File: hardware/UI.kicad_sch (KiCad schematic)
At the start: 1 part

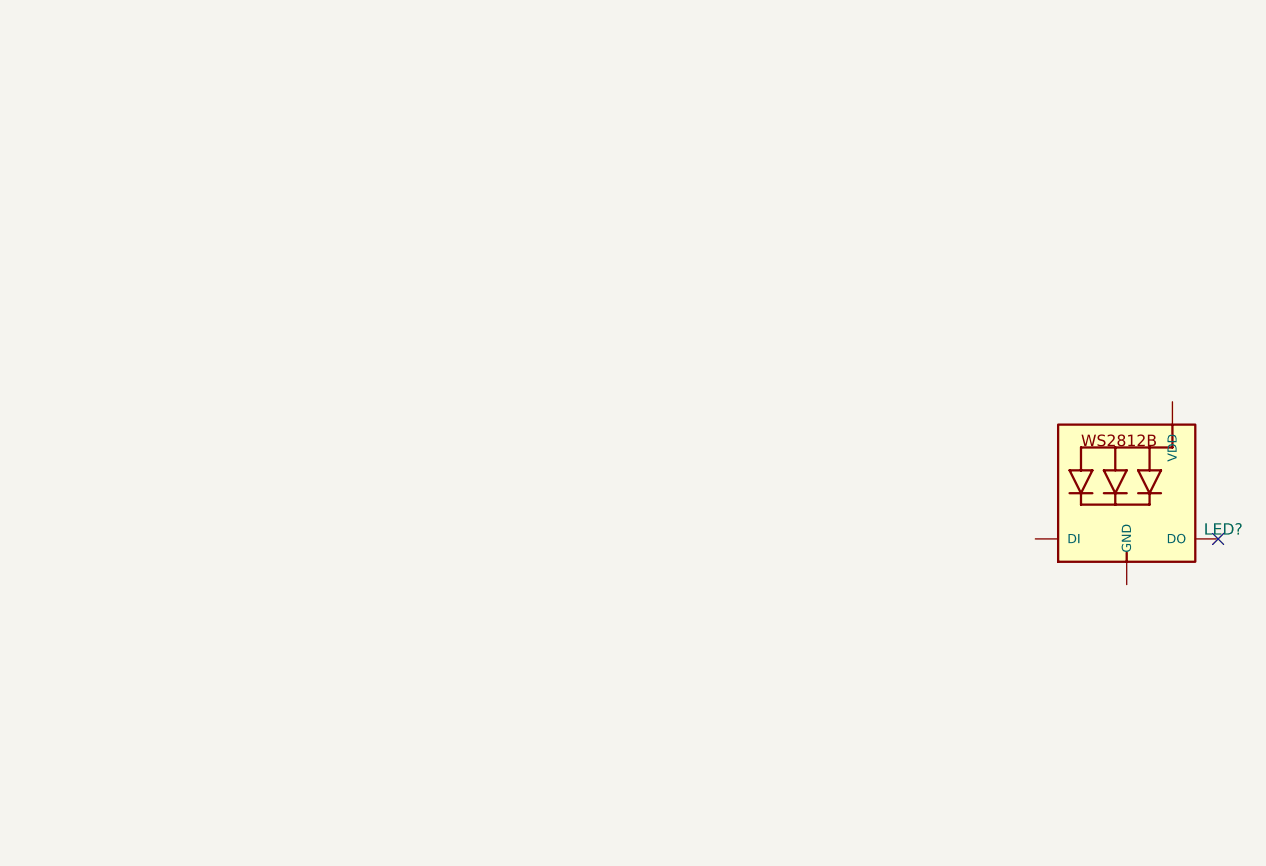
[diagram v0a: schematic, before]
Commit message: schematics finished, footprints assigned. Still need to fix foorptints for MOSFETS
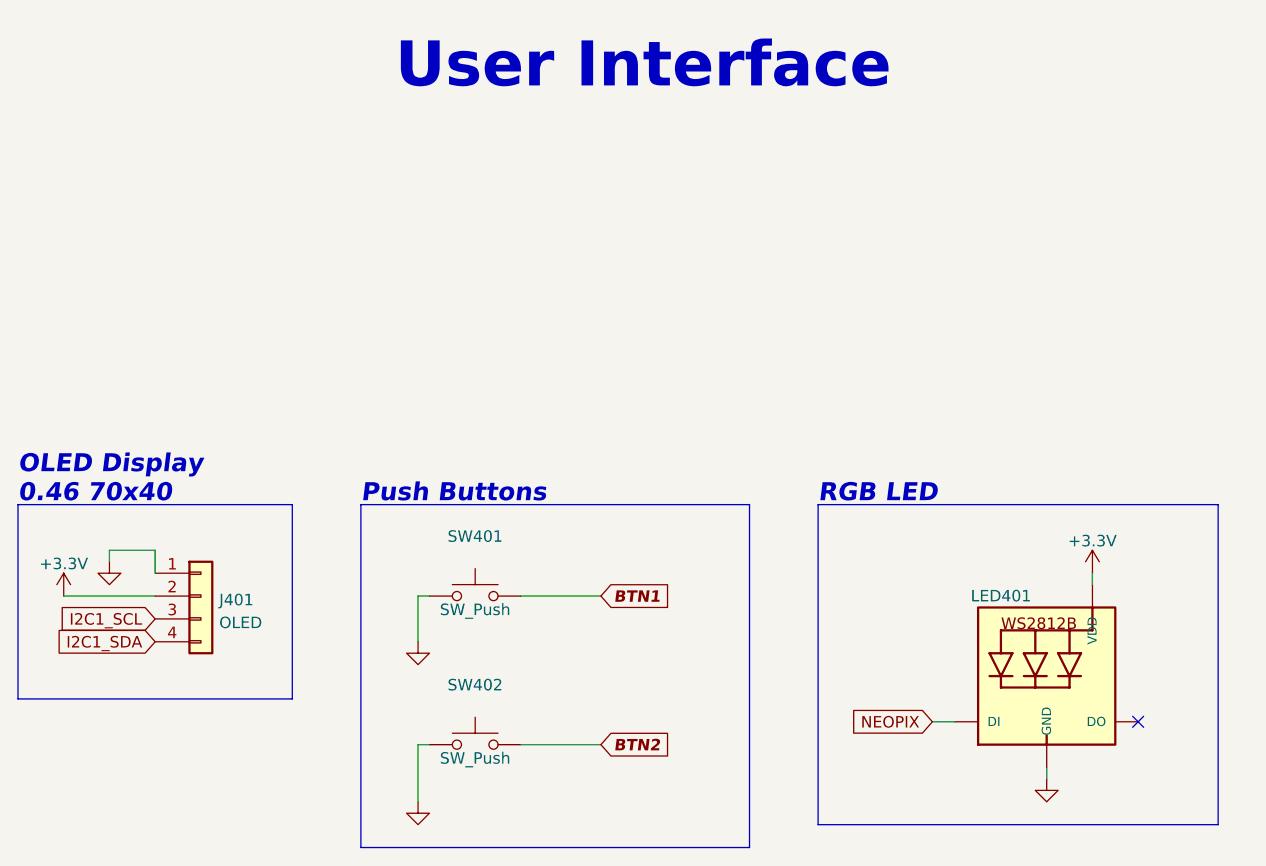
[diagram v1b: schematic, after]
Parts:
- added J401: OLED, Connector_PinHeader_2.54mm:PinHeader_1x04_P2.54mm_Vertical_SMD_Pin1Left, symbol Connector_Generic:Conn_01x04
- added SW401, SW402: SW_Push, STR-Switch:SW_SMD_SPST_8x3.6, symbol STR-Switches:SW_Push
- LED401: renamed from LED?; footprint (none) -> STR-LED:WS2812B; LCSC (none) -> C2761795; MANUFACTURER (none) -> WorldSemi; MFPN (none) -> WS2812B-B/W; MPN (none) -> WS2812B-B/W; Manufacturer (none) -> WorldSemi
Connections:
- new net +3V3: J401.2 (Pin_2), LED401.1 (VDD)
- new net BTN1: SW401.2
- new net BTN2: SW402.2
- new net GND: J401.1 (Pin_1), LED401.3 (GND), SW401.1, SW402.1
- new net I2C1_SCL: J401.3 (Pin_3)
- new net I2C1_SDA: J401.4 (Pin_4)
- new net NEOPIX: LED401.4 (DI)
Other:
- note added: "OLED Display 0.46 70x40"
- note added: "Push Buttons"
- note added: "RGB LED"
- note added: "User Interface"
- title: (none) -> SLA Chamber Hearter for Resin Printers
- moved on the sheet: LED401

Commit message: routing and foot print changes
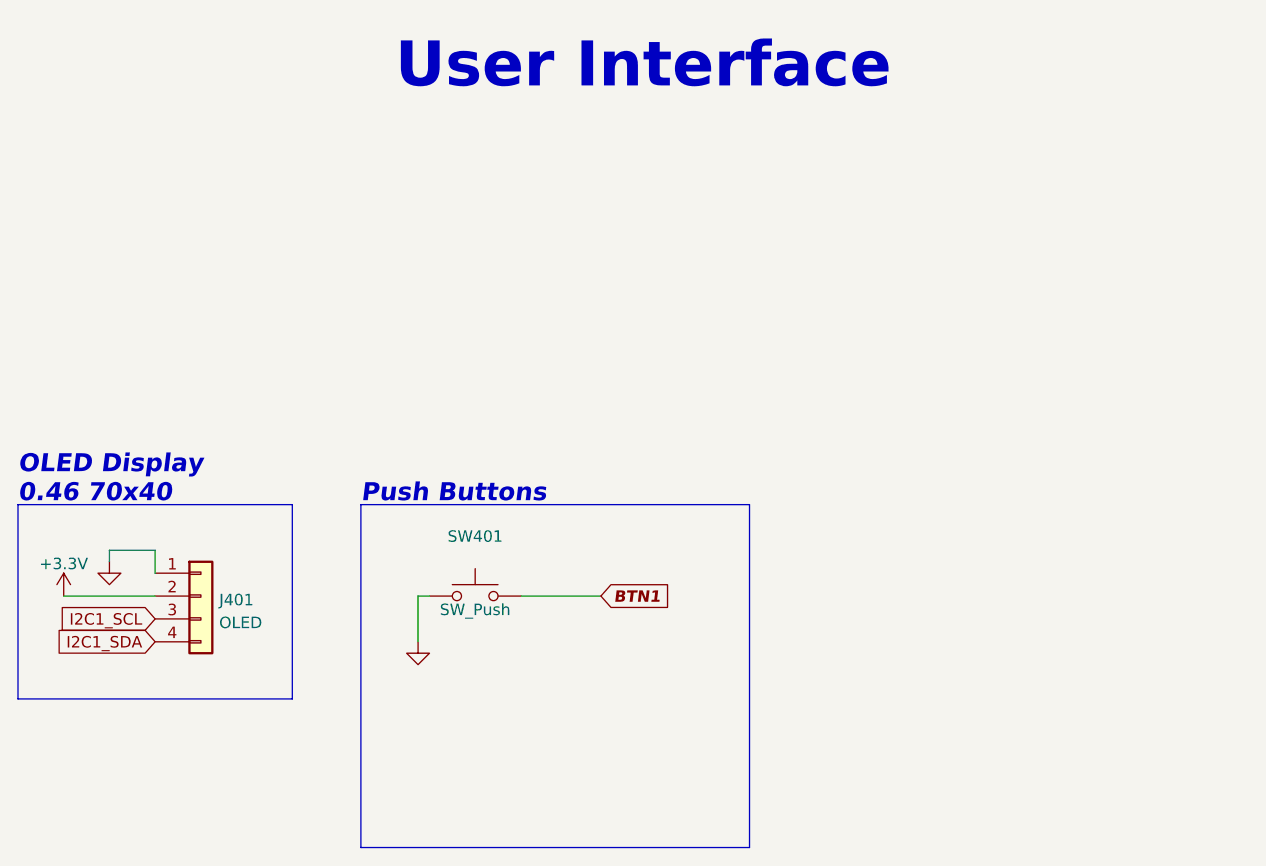
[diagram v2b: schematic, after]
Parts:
- removed LED401: WS2812B, STR-LED:WS2812B, symbol STR-LED:WS2812B
- removed SW402: SW_Push, STR-Switch:SW_SMD_SPST_8x3.6, symbol STR-Switches:SW_Push
- J401: footprint Connector_PinHeader_2.54mm:PinHeader_1x04_P2.54mm_Vertical_SMD_Pin1Left -> Connector_PinHeader_2.54mm:PinHeader_1x04_P2.54mm_Vertical
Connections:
- no-connect marks 1 -> 0
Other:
- note removed: "RGB LED"
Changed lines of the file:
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@@
     (comment 3 "License: CERN-OHL-P")
   )
-  (no_connect (at 204.47 107.95))
   (polyline (pts (xy 161.29 121.92) (xy 118.11 121.92))
     (stroke (width 0) (type default) (color 0 0 0 0))
@@
   )
   (polyline (pts (xy 80.01 83.82) (xy 110.49 83.82))
-    (stroke (width 0) (type default) (color 0 0 0 0))
-  )
-  (polyline (pts (xy 168.91 83.82) (xy 213.36 83.82))
-    (stroke (width 0) (type default) (color 0 0 0 0))
-  )
-  (wire (pts (xy 194.31 113.03) (xy 194.31 114.3))
-    (stroke (width 0) (type default) (color 0 0 0 0))
-  )
-  (wire (pts (xy 199.39 91.44) (xy 199.39 92.71))
-    (stroke (width 0) (type default) (color 0 0 0 0))
-  )
-  (polyline (pts (xy 213.36 83.82) (xy 213.36 119.38))
     (stroke (width 0) (type default) (color 0 0 0 0))
   )
@@
     (stroke (width 0) (type default) (color 0 0 0 0))
   )
-  (polyline (pts (xy 213.36 119.38) (xy 168.91 119.38))
-    (stroke (width 0) (type default) (color 0 0 0 0))
-  )
-  (polyline (pts (xy 168.91 83.82) (xy 168.91 119.38))
-    (stroke (width 0) (type default) (color 0 0 0 0))
-  )
   (wire (pts (xy 124.46 93.98) (xy 124.46 99.06))
     (stroke (width 0) (type default) (color 0 0 0 0))
@@
   )
   (wire (pts (xy 135.89 93.98) (xy 144.78 93.98))
-    (stroke (width 0) (type default) (color 0 0 0 0))
-  )
-  (wire (pts (xy 181.61 107.95) (xy 184.15 107.95))
-    (stroke (width 0) (type default) (color 0 0 0 0))
-  )
-  (wire (pts (xy 125.73 110.49) (xy 124.46 110.49))
     (stroke (width 0) (type default) (color 0 0 0 0))
   )
@@
     (stroke (width 0) (type default) (color 0 0 0 0))
   )
-  (wire (pts (xy 124.46 110.49) (xy 124.46 116.84))
-    (stroke (width 0) (type default) (color 0 0 0 0))
-  )
-  (wire (pts (xy 135.89 110.49) (xy 144.78 110.49))
-    (stroke (width 0) (type default) (color 0 0 0 0))
-  )
   (text "User Interface" (at 121.92 38.1 0)
     (effects (font (size 5 5) bold) (justify left bottom))
@@
   (text "OLED Display\n0.46 70x40" (at 80.01 83.82 0)
     (effects (font (size 2 2) bold italic) (justify left bottom))
-  )
-  (text "RGB LED" (at 168.91 83.82 0)
-    (effects (font (size 2 2) (thickness 0.4) bold italic) (justify left bottom))
-  )
-  (global_label "BTN2" (shape input) (at 144.78 110.49 0) (fields_autoplaced)
-    (effects (font (size 1.27 1.27) bold italic) (justify left))
-    (property "Intersheet References" "${INTERSHEET_REFS}" (id 0) (at 152.4167 110.363 0)
-      (effects (font (size 1.27 1.27) bold italic) (justify left) hide)
-    )
   )
   (global_label "I2C1_SDA" (shape input) (at 95.25 99.06 180) (fields_autoplaced)
@@
     (effects (font (size 1.27 1.27)) (justify right))
     (property "Intersheet References" "${INTERSHEET_REFS}" (id 0) (at 84.0679 96.4406 0)
-      (effects (font (size 1.27 1.27)) (justify right) hide)
-    )
-  )
-  (global_label "NEOPIX" (shape input) (at 181.61 107.95 180) (fields_autoplaced)
-    (effects (font (size 1.27 1.27)) (justify right))
-    (property "Intersheet References" "${INTERSHEET_REFS}" (id 0) (at 172.3026 107.8706 0)
       (effects (font (size 1.27 1.27)) (justify right) hide)
     )
@@
       (effects (font (size 1.27 1.27)) (justify left))
     )
-    (property "Footprint" "Connector_PinHeader_2.54mm:PinHeader_1x04_P2.54mm_Vertical_SMD_Pin1Left" (id 2) (at 100.33 93.98 0)
+    (property "Footprint" "Connector_PinHeader_2.54mm:PinHeader_1x04_P2.54mm_Vertical" (id 2) (at 100.33 93.98 0)
       (effects (font (size 1.27 1.27)) hide)
     )
@@
     (pin "1")
   )
-  (symbol (lib_id "STR-LED:WS2812B") (at 194.31 105.41 0) (unit 1)
-    (in_bom yes) (on_board yes)
-    (property "Reference" "LED401" (id 0) (at 189.23 93.98 0))
-    (property "Value" "WS2812B" (id 1) (at 196.85 113.03 0)
-      (effects (font (size 1.27 1.27)) (justify left bottom) hide)
-    )
-    (property "Footprint" "STR-LED:WS2812B" (id 2) (at 194.31 105.41 0)
-      (effects (font (size 1.27 1.27)) hide)
-    )
-    (property "Datasheet" "https://datasheet.lcsc.com/lcsc/2106062036_Worldsemi-WS2812B-B-W_C2761795.pdf" (id 3) (at 194.31 105.41 0)
-      (effects (font (size 1.27 1.27)) (justify left bottom) hide)
-    )
-    (property "Manufacturer" "WorldSemi" (id 4) (at 194.31 105.41 0)
-      (effects (font (size 1.27 1.27)) hide)
-    )
-    (property "MPN" "WS2812B-B/W" (id 5) (at 194.31 105.41 0)
-      (effects (font (size 1.27 1.27)) hide)
-    )
-    (property "LCSC" "C2761795" (id 6) (at 194.31 105.41 0)
-      (effects (font (size 1.27 1.27)) hide)
-    )
-    (property "MANUFACTURER" "WorldSemi" (id 7) (at 194.31 105.41 0)
-      (effects (font (size 1.27 1.27)) hide)
-    )
-    (property "MFPN" "WS2812B-B/W" (id 8) (at 194.31 105.41 0)
-      (effects (font (size 1.27 1.27)) hide)
-    )
-    (pin "1")
-    (pin "2")
-    (pin "3")
-    (pin "4")
-  )
   (symbol (lib_id "power:+3.3V") (at 85.09 93.98 0) (unit 1)
     (in_bom yes) (on_board yes) (fields_autoplaced)
@@
     (pin "1")
   )
-  (symbol (lib_id "power:GND") (at 194.31 114.3 0) (unit 1)
-    (in_bom yes) (on_board yes) (fields_autoplaced)
-    (property "Reference" "#PWR0403" (id 0) (at 194.31 120.65 0)
-      (effects (font (size 1.27 1.27)) hide)
-    )
-    (property "Value" "GND" (id 1) (at 194.31 118.7434 0)
-      (effects (font (size 1.27 1.27)) hide)
-    )
-    (property "Footprint" "" (id 2) (at 194.31 114.3 0)
-      (effects (font (size 1.27 1.27)) hide)
-    )
-    (property "Datasheet" "" (id 3) (at 194.31 114.3 0)
-      (effects (font (size 1.27 1.27)) hide)
-    )
-    (pin "1")
-  )
-  (symbol (lib_id "power:+3.3V") (at 199.39 91.44 0) (unit 1)
-    (in_bom yes) (on_board yes) (fields_autoplaced)
-    (property "Reference" "#PWR0404" (id 0) (at 199.39 95.25 0)
-      (effects (font (size 1.27 1.27)) hide)
-    )
-    (property "Value" "+3.3V" (id 1) (at 199.39 87.8642 0))
-    (property "Footprint" "" (id 2) (at 199.39 91.44 0)
-      (effects (font (size 1.27 1.27)) hide)
-    )
-    (property "Datasheet" "" (id 3) (at 199.39 91.44 0)
-      (effects (font (size 1.27 1.27)) hide)
-    )
-    (pin "1")
-  )
-  (symbol (lib_id "power:GND") (at 124.46 116.84 0) (unit 1)
-    (in_bom yes) (on_board yes) (fields_autoplaced)
-    (property "Reference" "#PWR0406" (id 0) (at 124.46 123.19 0)
-      (effects (font (size 1.27 1.27)) hide)
-    )
-    (property "Value" "GND" (id 1) (at 124.46 121.2834 0)
-      (effects (font (size 1.27 1.27)) hide)
-    )
-    (property "Footprint" "" (id 2) (at 124.46 116.84 0)
-      (effects (font (size 1.27 1.27)) hide)
-    )
-    (property "Datasheet" "" (id 3) (at 124.46 116.84 0)
-      (effects (font (size 1.27 1.27)) hide)
-    )
-    (pin "1")
-  )
-  (symbol (lib_id "STR-Switches:SW_Push") (at 130.81 110.49 0) (unit 1)
-    (in_bom yes) (on_board yes)
-    (property "Reference" "SW402" (id 0) (at 130.81 103.8692 0))
-    (property "Value" "SW_Push" (id 1) (at 130.81 112.014 0))
-    (property "Footprint" "STR-Switch:SW_SMD_SPST_8x3.6" (id 2) (at 130.81 105.41 0)
-      (effects (font (size 1.27 1.27)) hide)
-    )
-    (property "Datasheet" "~" (id 3) (at 130.81 105.41 0)
-      (effects (font (size 1.27 1.27)) hide)
-    )
-    (pin "1")
-    (pin "2")
-  )
   (symbol (lib_id "power:GND") (at 124.46 99.06 0) (unit 1)
